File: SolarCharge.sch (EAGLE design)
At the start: 20 parts, among them U1 TINY4/5/9/10-TSHR/TS8R, U2 TINY4/5/9/10-TSHR/TS8R

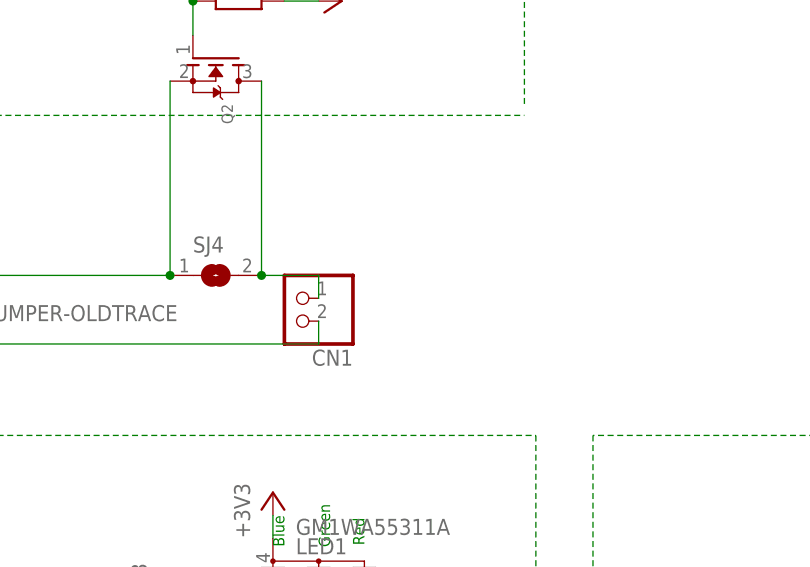
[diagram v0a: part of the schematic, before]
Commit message: Solar out to 3V3 solderjumper
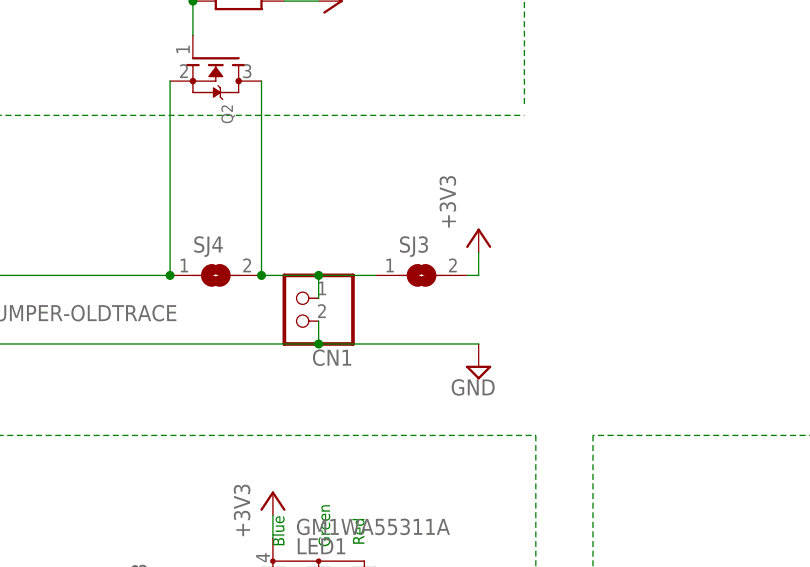
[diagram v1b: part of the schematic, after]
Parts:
- added SJ3: (no value), jumper:SJ
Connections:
- net +3V3: now also SJ3.2
- net N$9: now also SJ3.1
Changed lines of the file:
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@@
 <setting verticaltext="up"/>
 </settings>
-<grid distance="0.05" unitdist="inch" unit="inch" style="lines" multiple="1" display="no" altdistance="0.01" altunitdist="inch" altunit="inch"/>
+<grid distance="0.1" unitdist="inch" unit="inch" style="lines" multiple="1" display="no" altdistance="0.01" altunitdist="inch" altunit="inch"/>
 <layers>
 <layer number="1" name="Top" color="4" fill="1" visible="no" active="no"/>
@@
 <part name="+3V5" library="supply1" deviceset="+3V3" device=""/>
 <part name="SJ4" library="jumper" library_urn="urn:adsk.eagle:library:252" deviceset="SJ" device="" package3d_urn="urn:adsk.eagle:package:15471/1"/>
+<part name="+3V6" library="supply1" deviceset="+3V3" device=""/>
+<part name="SUPPLY3" library="supply2" library_urn="urn:adsk.eagle:library:372" deviceset="GND" device=""/>
+<part name="SJ3" library="jumper" library_urn="urn:adsk.eagle:library:252" deviceset="SJ" device="" package3d_urn="urn:adsk.eagle:package:15471/1"/>
 </parts>
 <sheets>
@@
 <attribute name="VALUE" x="125.73" y="77.47" size="1.778" layer="96"/>
 </instance>
+<instance part="+3V6" gate="G$1" x="157.48" y="86.36" smashed="yes">
+<attribute name="VALUE" x="154.94" y="86.36" size="1.778" layer="96" rot="R90"/>
+</instance>
+<instance part="SUPPLY3" gate="GND" x="157.48" y="71.12" smashed="yes" rot="MR0">
+<attribute name="VALUE" x="159.385" y="67.945" size="1.778" layer="96" rot="MR0"/>
+</instance>
+<instance part="SJ3" gate="1" x="151.13" y="81.28" smashed="yes">
+<attribute name="NAME" x="148.59" y="83.82" size="1.778" layer="95"/>
+<attribute name="VALUE" x="148.59" y="77.47" size="1.778" layer="96"/>
+</instance>
 </instances>
 <busses>
@@
 <wire x1="139.7" y1="73.66" x2="101.6" y2="73.66" width="0.1524" layer="91"/>
 <junction x="101.6" y="73.66"/>
+<pinref part="SUPPLY3" gate="GND" pin="GND"/>
+<wire x1="157.48" y1="73.66" x2="139.7" y2="73.66" width="0.1524" layer="91"/>
+<junction x="139.7" y="73.66"/>
 </segment>
 <segment>
@@
 <wire x1="127" y1="142.24" x2="127" y2="143.51" width="0.1524" layer="91"/>
 </segment>
+<segment>
+<pinref part="+3V6" gate="G$1" pin="+3V3"/>
+<wire x1="157.48" y1="83.82" x2="157.48" y2="81.28" width="0.1524" layer="91"/>
+<pinref part="SJ3" gate="1" pin="2"/>
+<wire x1="156.21" y1="81.28" x2="157.48" y2="81.28" width="0.1524" layer="91"/>
+</segment>
 </net>
 <net name="RED_RESISTOR" class="0">
@@
 </segment>
 </net>
+<net name="N$10" class="0">
+<segment>
+<pinref part="R4" gate="G$1" pin="1"/>
+<pinref part="Q2" gate="G$1" pin="G"/>
+<wire x1="125.73" y1="111.76" x2="125.73" y2="107.95" width="0.1524" layer="91"/>
+<pinref part="U2" gate="G$1" pin="(PCINT0/TPIDATA/OC0A/ADC0/AIN0)PB0"/>
+<wire x1="125.73" y1="124.46" x2="125.73" y2="111.76" width="0.1524" layer="91"/>
+<junction x="125.73" y="111.76"/>
+</segment>
+</net>
+<net name="N$11" class="0">
+<segment>
+<pinref part="U2" gate="G$1" pin="(RESET/PCINT3/ADC3)PB3"/>
+<pinref part="R5" gate="G$1" pin="2"/>
+<wire x1="125.73" y1="132.08" x2="127" y2="132.08" width="0.1524" layer="91"/>
+</segment>
+</net>
 <net name="N$9" class="0">
 <segment>
@@
 <pinref part="SJ4" gate="1" pin="2"/>
 <junction x="133.35" y="81.28"/>
-</segment>
-</net>
-<net name="N$10" class="0">
-<segment>
-<pinref part="R4" gate="G$1" pin="1"/>
-<pinref part="Q2" gate="G$1" pin="G"/>
-<wire x1="125.73" y1="111.76" x2="125.73" y2="107.95" width="0.1524" layer="91"/>
-<pinref part="U2" gate="G$1" pin="(PCINT0/TPIDATA/OC0A/ADC0/AIN0)PB0"/>
-<wire x1="125.73" y1="124.46" x2="125.73" y2="111.76" width="0.1524" layer="91"/>
-<junction x="125.73" y="111.76"/>
-</segment>
-</net>
-<net name="N$11" class="0">
-<segment>
-<pinref part="U2" gate="G$1" pin="(RESET/PCINT3/ADC3)PB3"/>
-<pinref part="R5" gate="G$1" pin="2"/>
-<wire x1="125.73" y1="132.08" x2="127" y2="132.08" width="0.1524" layer="91"/>
-</segment>
-</net>
+<pinref part="SJ3" gate="1" pin="1"/>
+<wire x1="146.05" y1="81.28" x2="139.7" y2="81.28" width="0.1524" layer="91"/>
+<junction x="139.7" y="81.28"/>
+</segment>
+</net>

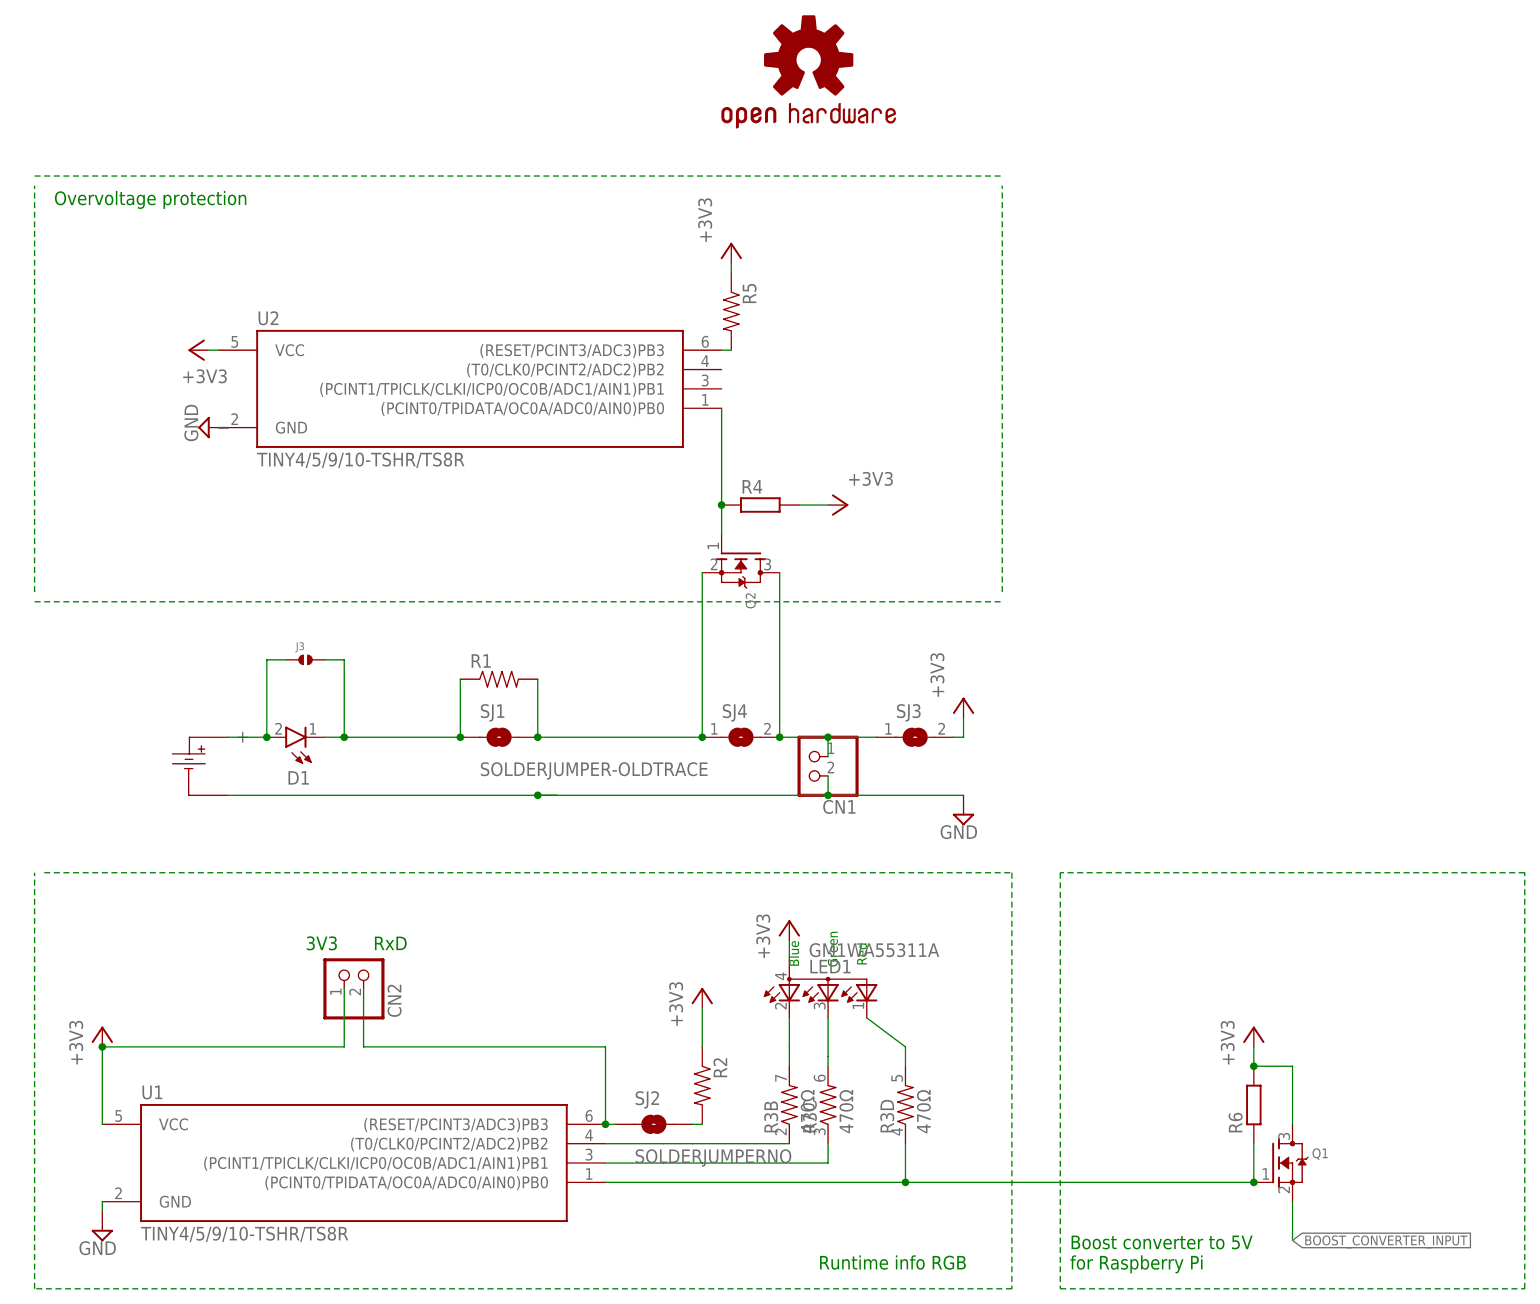
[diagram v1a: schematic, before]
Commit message: Use XC2606 LDO instead of Tiny10
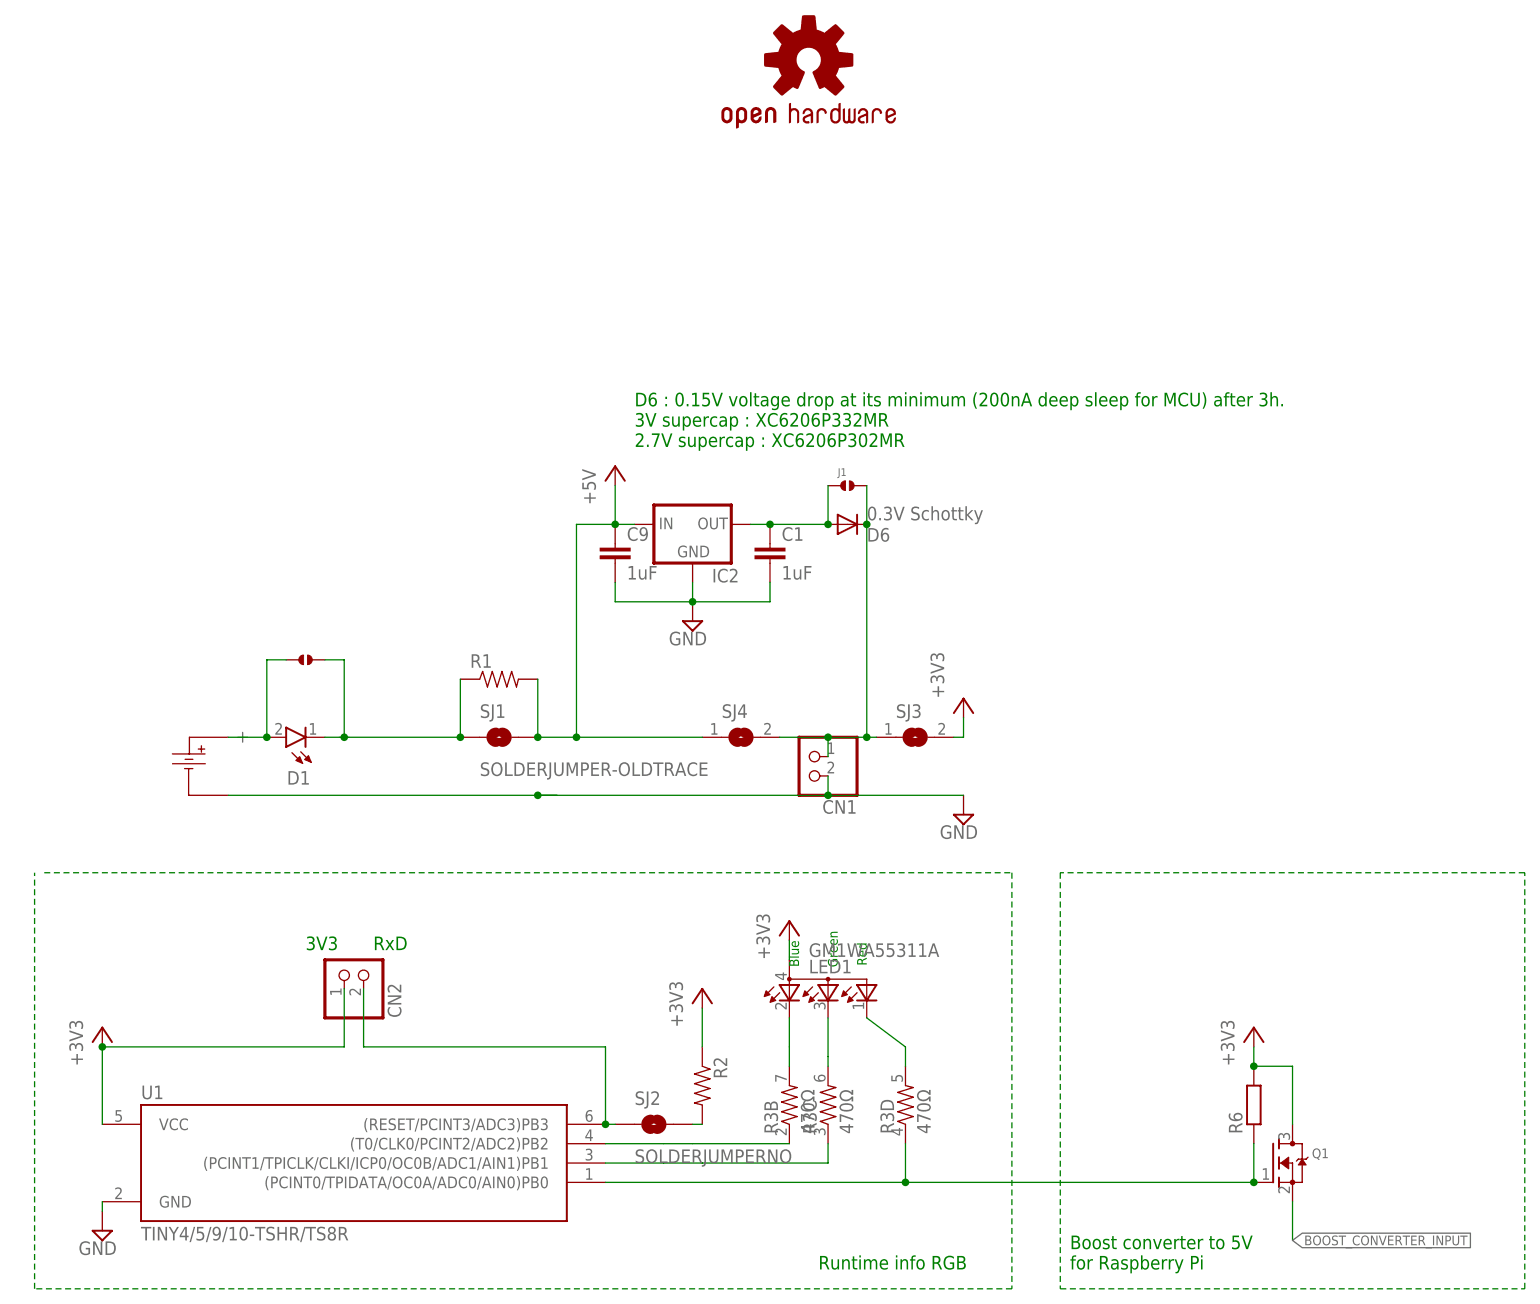
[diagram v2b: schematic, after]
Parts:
- removed Q2: (no value), adafruit:MOSFET-NREFLOW
- removed R4: (no value), rcl:R-EU_R0603
- removed R5: (no value), ROHM:RESISTOR0603-RES
- removed U2: TINY4/5/9/10-TSHR/TS8R, bt_avr:TINY4/5/9/10-TSHR/TS8R
- added C1, C9: 1uF, rcl:C-EUC0603
- added D6: 0.3V Schottky, diode:DIODE-SOD523
- added IC2: (no value), MCP1700:MCP1700TT
- added J1: (no value), solderjumper:SOLDERJUMPER.2.MED
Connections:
- removed net N$10: Q2.G, R4.1, U2.(PCINT0/TPIDATA/OC0A/ADC0/AIN0)PB0
- removed net N$11: R5.2, U2.(RESET/PCINT3/ADC3)PB3
- removed net N$9: CN1.2, Q2.D, SJ3.1, SJ4.2
- new net +5V: C9.1, IC2.IN, R1.2, SJ1.2, SJ4.1
- new net N$25: C1.1, D6.A, IC2.OUT, J1.1
- net +3V3: no longer R4.2, R5.1, U2.VCC
- net GND: now also C1.2, C9.2, IC2.GND; no longer U2.GND
- net N$4: now also CN1.2, D6.C, J1.2, SJ3.1, SJ4.2; no longer Q2.S, R1.2, SJ1.2, SJ4.1
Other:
- note added: "D6 : 0.15V voltage drop at its minimum (200nA deep sleep for MCU) after 3h. 3V supercap : XC6206P332MR 2.7V supercap : XC6206P302MR"
- note removed: "Overvoltage protection"

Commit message: Add info on how to draw ellipse in brd
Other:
- note added: "How to draw ellipse shape for board: Go To File->Run Ulp. Choose cmd-draw.ulp Choose Polygon and Full ellipse. For this board, Width: 0.15 X: 20 Y: 31 Radius: 21 Angle Step: 0.1 Ellipse Factor: 2"
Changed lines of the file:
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@@
 3V supercap : XC6206P332MR
 2.7V supercap : XC6206P302MR</text>
+<text x="33.02" y="124.46" size="2.54" layer="91">How to draw ellipse shape for board:
+Go To File-&gt;Run Ulp. Choose cmd-draw.ulp
+Choose Polygon and Full ellipse. For this board,
+Width: 0.15 X: 20 Y: 31
+Radius: 21 Angle Step: 0.1
+Ellipse Factor: 2</text>
 </plain>
 <instances>

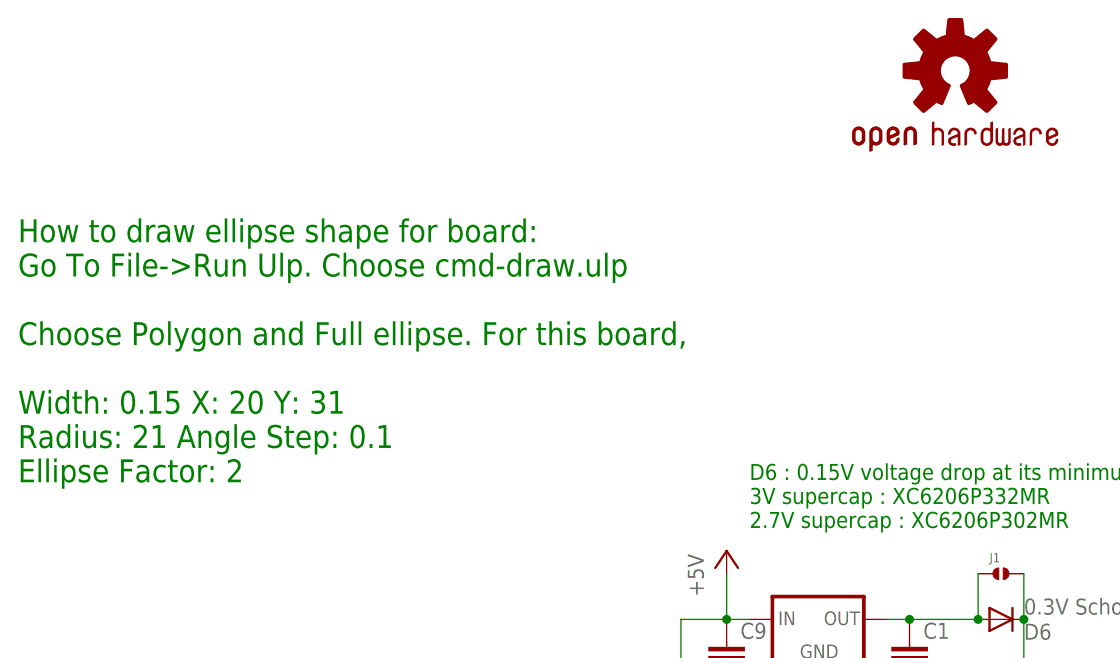
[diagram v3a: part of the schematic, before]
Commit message: Add ref to online ellipse from cylinder section calculator
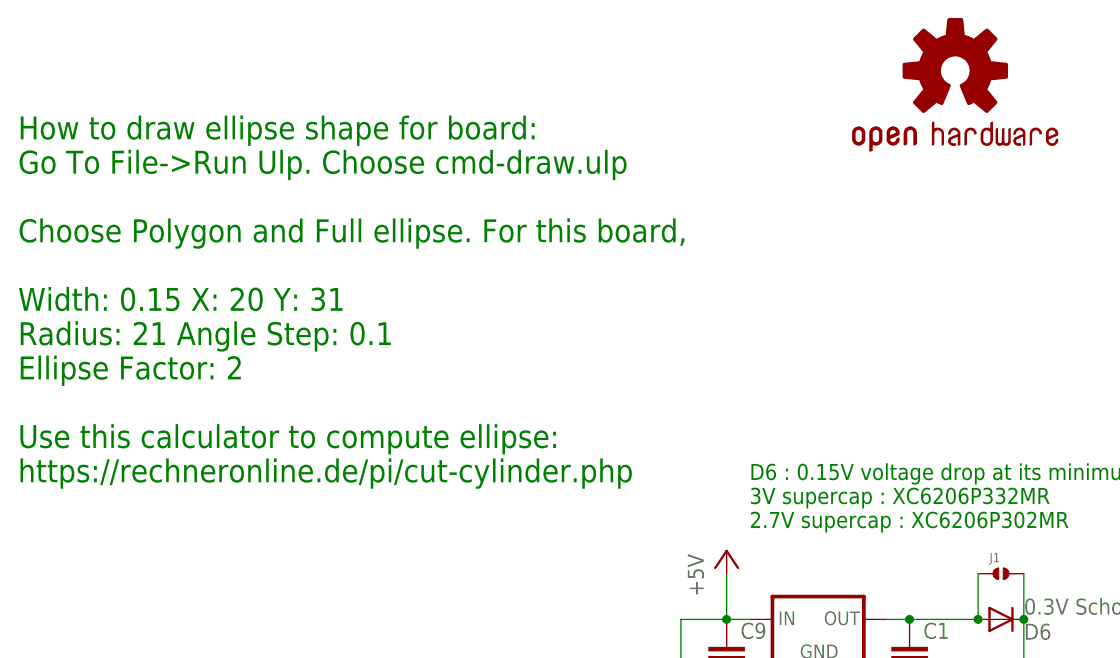
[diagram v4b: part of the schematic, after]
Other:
- note added: "How to draw ellipse shape for board: Go To File->Run Ulp. Choose cmd-draw.ulp Choose Polygon and Full ellipse. For this board, Width: 0.15 X: 20 Y: 31 Radius: 21 Angle Step: 0.1 Ellipse Factor: 2 Use this calculator to compute ellipse: https://rechneronline.de/pi/cut-cylinder.php"
- note removed: "How to draw ellipse shape for board: Go To File->Run Ulp. Choose cmd-draw.ulp Choose Polygon and Full ellipse. For this board, Width: 0.15 X: 20 Y: 31 Radius: 21 Angle Step: 0.1 Ellipse Factor: 2"
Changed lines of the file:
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@@
 Width: 0.15 X: 20 Y: 31
 Radius: 21 Angle Step: 0.1
-Ellipse Factor: 2</text>
+Ellipse Factor: 2
+Use this calculator to compute ellipse:
+https://rechneronline.de/pi/cut-cylinder.php</text>
 </plain>
 <instances>

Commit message: Edit ellipse generation description
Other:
- note added: "How to draw ellipse shape for board: Go To File->Run Ulp. Choose cmd-draw.ulp Choose Wir, Angle Step and Full ellipse. For this board, Width: 0.1524 X: 20 Y: 31 Radius: 23 Angle Step: 0.1 Ellipse Factor: 2 Use this calculator to compute ellipse: https://rechneronline.de/pi/cut-cylinder.php"
- note removed: "How to draw ellipse shape for board: Go To File->Run Ulp. Choose cmd-draw.ulp Choose Polygon and Full ellipse. For this board, Width: 0.15 X: 20 Y: 31 Radius: 21 Angle Step: 0.1 Ellipse Factor: 2 Use this calculator to compute ellipse: https://rechneronline.de/pi/cut-cylinder.php"
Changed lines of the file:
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@@
 <text x="33.02" y="124.46" size="2.54" layer="91">How to draw ellipse shape for board:
 Go To File-&gt;Run Ulp. Choose cmd-draw.ulp
-Choose Polygon and Full ellipse. For this board,
-Width: 0.15 X: 20 Y: 31
-Radius: 21 Angle Step: 0.1
+Choose Wir, Angle Step and Full ellipse. For this board,
+Width: 0.1524 X: 20 Y: 31
+Radius: 23 Angle Step: 0.1
 Ellipse Factor: 2
 Use this calculator to compute ellipse:
